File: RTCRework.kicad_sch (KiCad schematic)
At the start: 6 parts, among them J1 Conn_01x01, J2 Conn_01x01, U1 RT9058-33GV

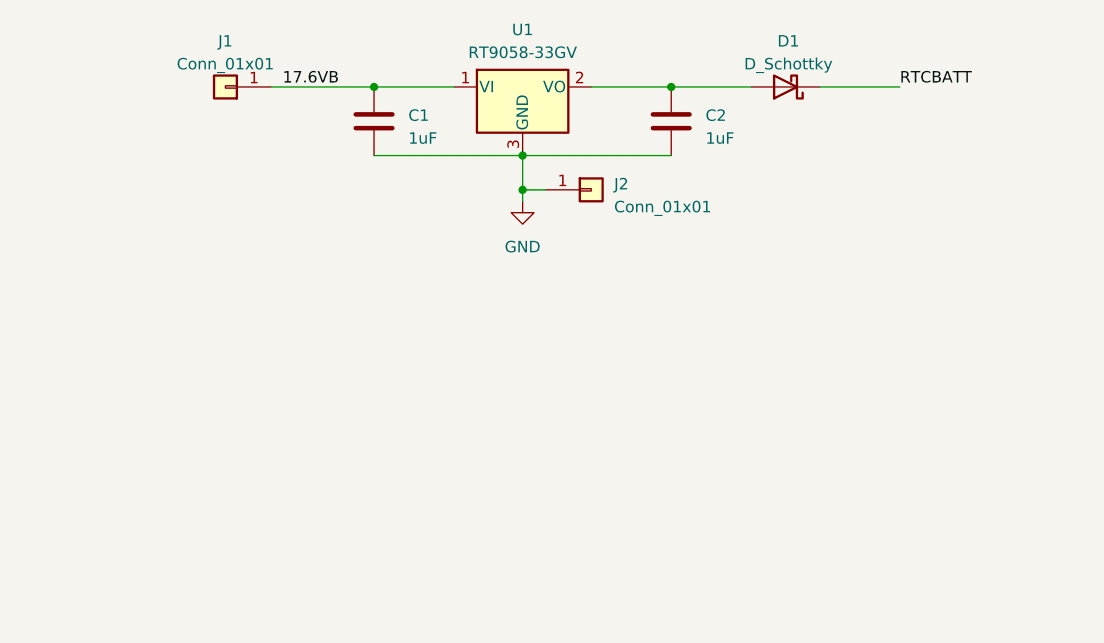
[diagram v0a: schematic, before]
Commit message: Add fuse, switch to smaller packages
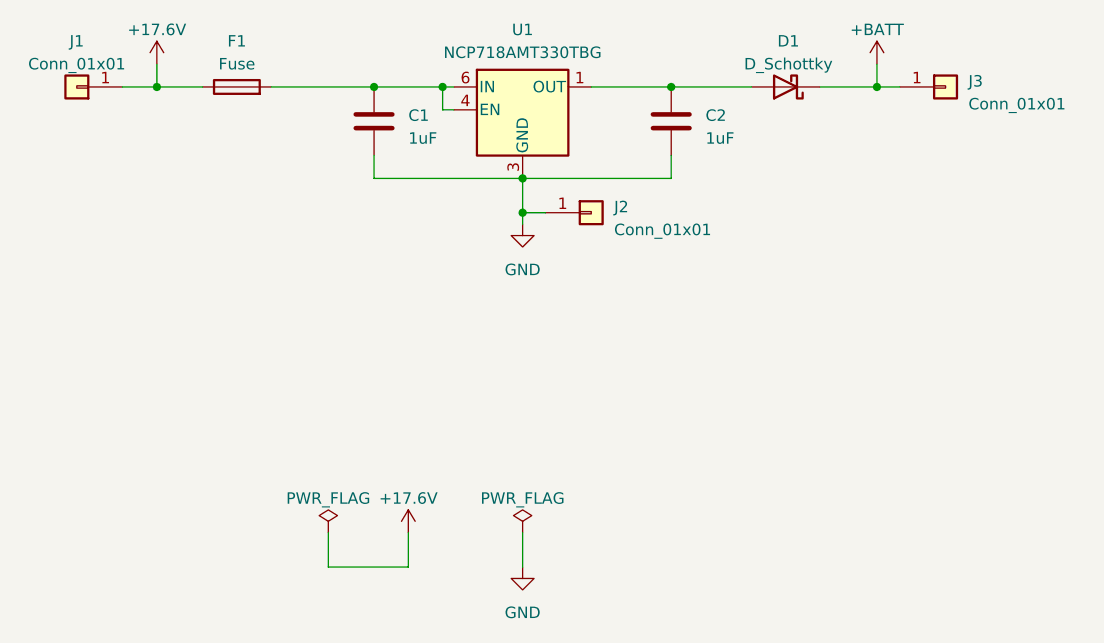
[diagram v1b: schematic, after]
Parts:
- removed U1: RT9058-33GV, Package_TO_SOT_SMD:SOT-23, symbol Regulator_Linear:AP7384-33SA
- added F1: Fuse, Fuse:Fuse_0402_1005Metric, symbol Device:Fuse
- added J3: Conn_01x01, symbol Connector_Generic:Conn_01x01
- added U1: NCP718AMT330TBG, Package_SON:WSON-6-1EP_2x2mm_P0.65mm_EP1x1.6mm, symbol Regulator_Linear:TLV75533PDRV
- C1, C2: footprint Capacitor_SMD:C_0603_1608Metric -> Capacitor_SMD:C_0402_1005Metric
- D1: footprint Diode_SMD:D_0603_1608Metric -> Diode_SMD:D_0402_1005Metric
- J1: footprint TestPoint:TestPoint_Pad_2.0x2.0mm -> TestPoint:TestPoint_Pad_3.0x3.0mm
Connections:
- net GND: now also U1.3 (GND), U1.7 (GND)
- net at C2.1, D1.2 (A): now also U1.1 (OUT)
- net 17.6VB: no longer names the net of C1.1
- net 17.6VB: now also F1.2, U1.4 (EN), U1.6 (IN); no longer J1.1 (Pin_1)
- net RTCBATT renamed +BATT
- net +BATT: now also J3.1 (Pin_1)
- new net +17.6V: F1.1, J1.1 (Pin_1)
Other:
- moved on the sheet: J1, J2
